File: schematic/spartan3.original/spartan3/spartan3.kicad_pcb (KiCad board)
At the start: 2 copper layers, 200 x 160 mm, 208 parts, among them U1_clk_select_0 SPFT_Sliding_Switch-dynacore, U2 XC3S250E-4TQG144C

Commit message: PCB layout :: updated
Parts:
- moved R_out_can_read_0 159.0 mm to (42.2, 5.08)
- moved R_out_can_write_0 139.3 mm to (83.8, 7.62)
- moved R_JTAG_TDO_0 133.7 mm to (152.4, 15.2)
- moved R_in_bus1_0 132.3 mm to (20.3, 55.9)
- moved R_eeprom_w_0 118.1 mm to (175.3, 7.62)
- moved R_eeprom_s_0 116.3 mm to (167.6, 15.2)
- moved R_in_write_reg_en_0 116.2 mm to (94.0, 12.7)
- moved R__eeprom_dq1_0 113.0 mm to (167.6, 20.3)
- moved R_out_clkr_0 110.1 mm to (12.7, 132.1)
- moved R_out_temp_w_0 108.1 mm to (208.3, 121.9)
- moved D_in_bus1_one_0 107.1 mm to (29.5, 96.5)
- moved R_in_is_clk_high_0 105.0 mm to (45.7, 151.9)
- moved R_in_clk_manual_0 102.6 mm to (45.7, 157.5)
- moved R_in_manual_input_r_0 97.9 mm to (185.4, 88.9)
- moved R_in_is_clk_low_0 97.2 mm to (45.7, 147.3)
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
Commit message: PCB layout :: updated
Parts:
- moved R_out_sysbus_6 231.5 mm to (224.5, 142.2)
- moved D_out_sysbus_6 213.9 mm to (236.2, 142.2)
- moved D_out_sysbus_4 213.1 mm to (236.2, 132.1)
- moved D_out_sysbus_2 211.6 mm to (236.2, 121.9)
- moved D_out_sysbus_0 209.4 mm to (235.2, 111.8)
- moved D_out_sysbus_7 208.2 mm to (235.2, 147.3)
- moved D_out_sysbus_3 204.1 mm to (235.2, 127.0)
- moved C_clk_1 197.3 mm to (213.4, 58.4)
- moved L_clk_0 196.4 mm to (221.0, 58.4)
- moved D_out_sysbus_5 191.5 mm to (236.2, 137.2)
- moved R_eeprom_hold_0 158.3 mm to (177.8, 2.54)
- moved D_out_r1_r_0 151.2 mm to (116.8, 236.2)
- moved D_in_manual_input_r_0 148.7 mm to (195.6, 185.4)
- moved D_out_ram_w_0 145.2 mm to (116.8, 243.8)
- moved D_out_acc_r_0 144.0 mm to (119.4, 251.5)
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
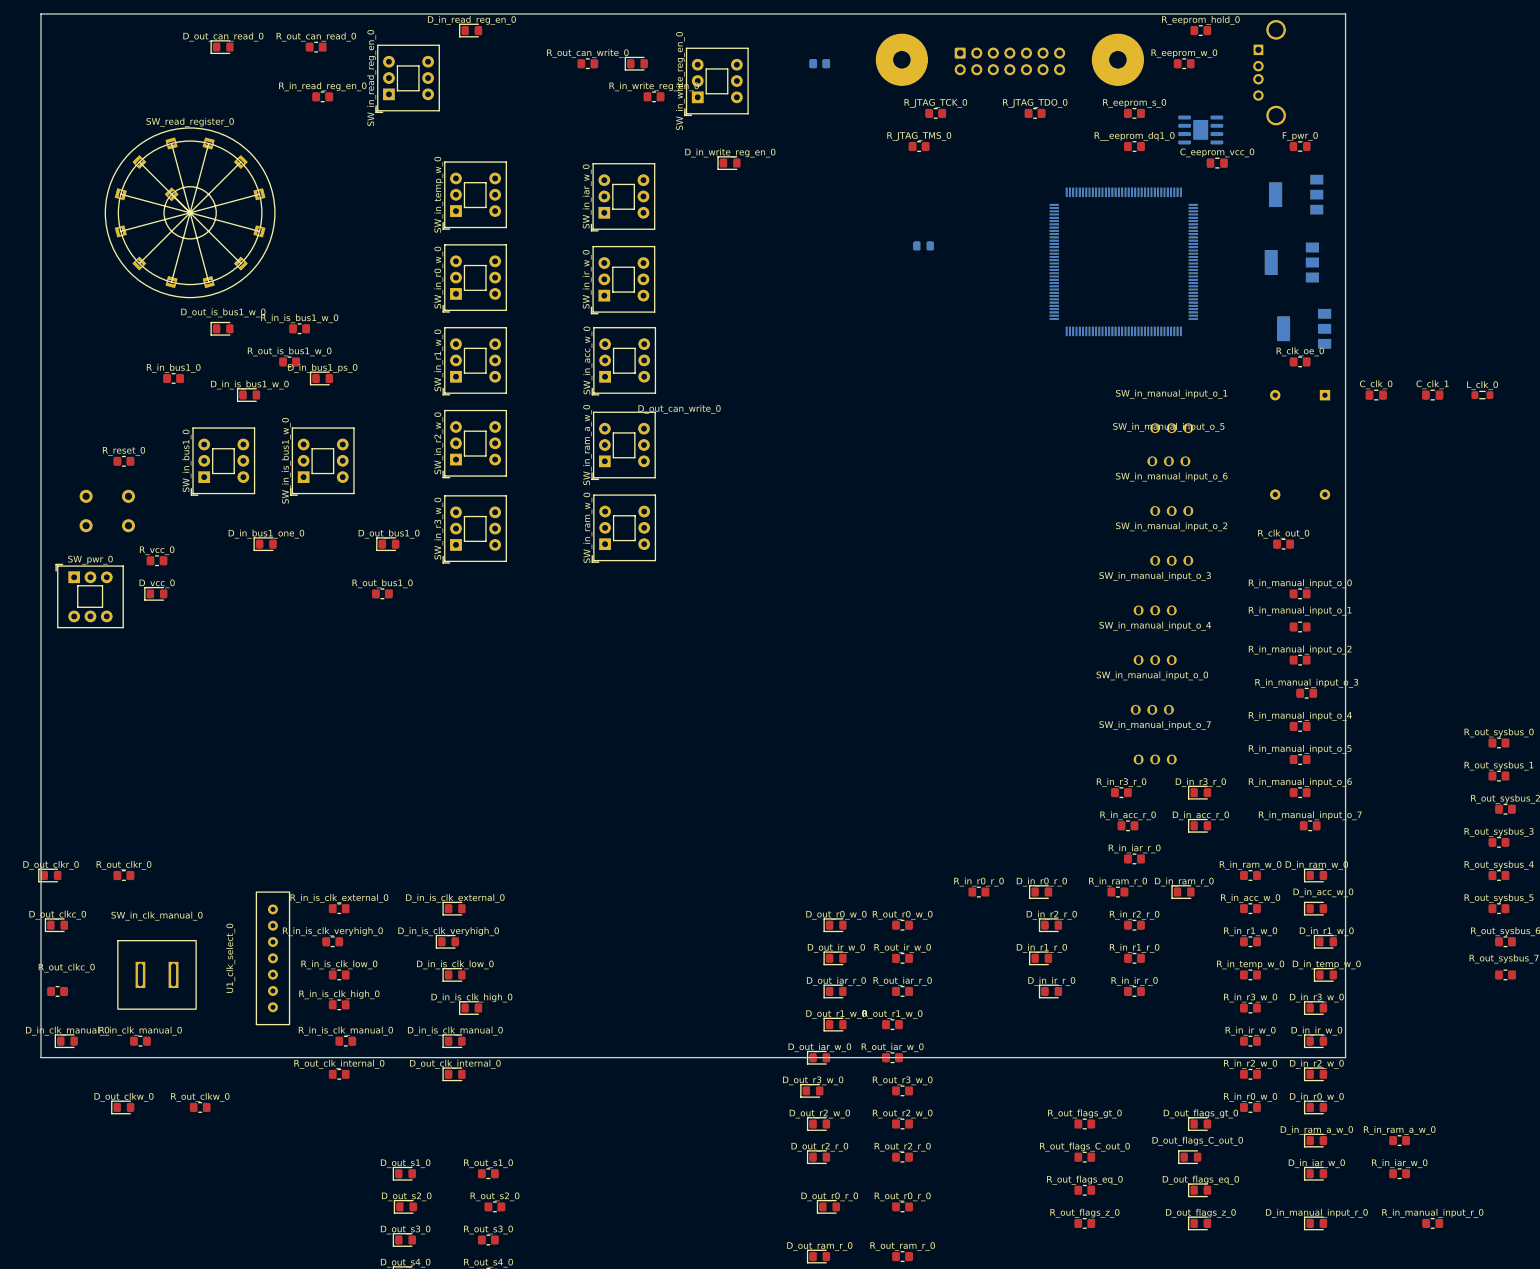
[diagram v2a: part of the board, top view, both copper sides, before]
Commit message: Schematics :: Read Register fixed -- Rs added. PCB layout :: Updated
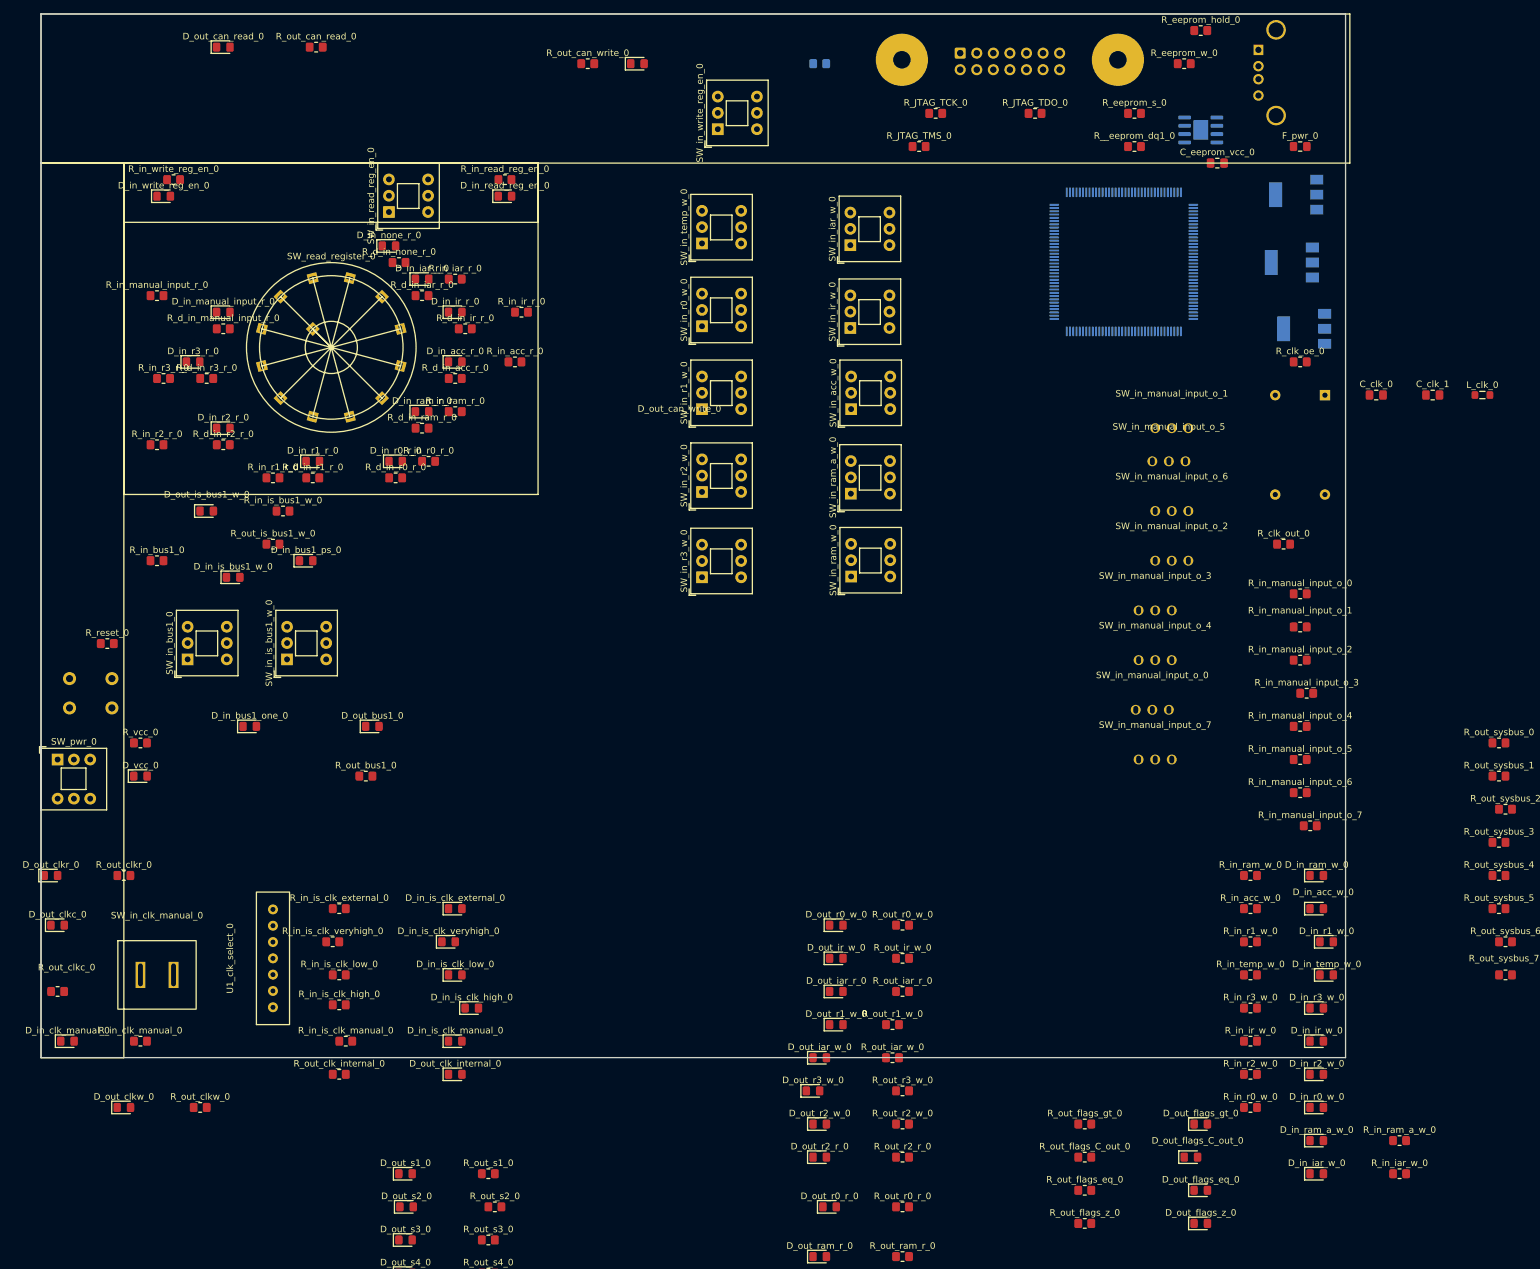
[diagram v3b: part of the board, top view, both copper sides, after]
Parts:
- added D_in_none_r_0: LED_Small, LED_SMD:LED_0805_2012Metric_Pad1.15x1.40mm_HandSolder, F.Cu at (53.3, 35.6)
- added R_d_in_acc_r_0: 100R, Resistor_SMD:R_0805_2012Metric_Pad1.20x1.40mm_HandSolder, F.Cu at (63.5, 55.9)
- added R_d_in_iar_r_0: 100R, Resistor_SMD:R_0805_2012Metric_Pad1.20x1.40mm_HandSolder, F.Cu at (58.4, 43.2)
- added R_d_in_ir_r_0: 100R, Resistor_SMD:R_0805_2012Metric_Pad1.20x1.40mm_HandSolder, F.Cu at (65.0, 48.3)
- added R_d_in_manual_input_r_0: 100R, Resistor_SMD:R_0805_2012Metric_Pad1.20x1.40mm_HandSolder, F.Cu at (27.9, 48.3)
- added R_d_in_none_r_0: 100R, Resistor_SMD:R_0805_2012Metric_Pad1.20x1.40mm_HandSolder, F.Cu at (54.9, 38.1)
- added R_d_in_r0_r_0: 100R, Resistor_SMD:R_0805_2012Metric_Pad1.20x1.40mm_HandSolder, F.Cu at (54.4, 71.1)
- added R_d_in_r1_r_0: 100R, Resistor_SMD:R_0805_2012Metric_Pad1.20x1.40mm_HandSolder, F.Cu at (41.7, 71.1)
- added R_d_in_r2_r_0: 100R, Resistor_SMD:R_0805_2012Metric_Pad1.20x1.40mm_HandSolder, F.Cu at (27.9, 66.0)
- added R_d_in_r3_r_0: 100R, Resistor_SMD:R_0805_2012Metric_Pad1.20x1.40mm_HandSolder, F.Cu at (25.4, 55.9)
- added R_d_in_ram_r_0: 100R, Resistor_SMD:R_0805_2012Metric_Pad1.20x1.40mm_HandSolder, F.Cu at (58.4, 63.5)
- D_in_iar_r_0: moved to F.Cu
- moved R_in_manual_input_r_0 241.8 mm to (17.8, 43.2)
- moved D_in_manual_input_r_0 218.2 mm to (27.9, 45.7)
- moved D_in_r3_r_0 168.0 mm to (23.3, 53.3)
- moved R_in_r2_r_0 167.0 mm to (17.8, 66.0)
- moved R_in_r3_r_0 160.0 mm to (18.8, 55.9)
- moved R_in_r1_r_0 151.2 mm to (35.6, 71.1)
- moved D_in_r2_r_0 148.1 mm to (27.9, 63.5)
- moved R_in_ir_r_0 140.3 mm to (73.7, 45.7)
- moved D_in_ir_r_0 138.6 mm to (63.5, 45.7)
- moved D_in_ram_r_0 138.1 mm to (58.4, 61.0)
- moved R_in_iar_r_0 136.9 mm to (63.5, 40.6)
- moved D_in_r1_r_0 135.3 mm to (41.7, 68.6)
- moved D_in_acc_r_0 134.6 mm to (63.5, 53.3)
- moved R_in_ram_r_0 125.5 mm to (63.5, 61.0)
- moved D_in_r0_r_0 119.1 mm to (54.4, 68.6)
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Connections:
- D_in_acc_r_0 pad 2: VCC -> Net-(D_in_acc_r_0-Pad2)
- D_in_iar_r_0 pad 2: VCC -> Net-(D_in_iar_r_0-Pad2)
- D_in_ir_r_0 pad 2: VCC -> Net-(D_in_ir_r_0-Pad2)
- D_in_manual_input_r_0 pad 2: VCC -> Net-(D_in_manual_input_r_0-Pad2)
- D_in_r0_r_0 pad 2: VCC -> Net-(D_in_r0_r_0-Pad2)
- D_in_r1_r_0 pad 2: VCC -> Net-(D_in_r1_r_0-Pad2)
- D_in_r2_r_0 pad 2: VCC -> Net-(D_in_r2_r_0-Pad2)
- D_in_r3_r_0 pad 2: VCC -> Net-(D_in_r3_r_0-Pad2)
- D_in_ram_r_0 pad 2: VCC -> Net-(D_in_ram_r_0-Pad2)
- SW_read_register_0 pad 1: in_iar_r -> in_manual_input_r
- SW_read_register_0 pad 10: unconnected-(SW_read_register_0-Pad10) -> in_r1_r
- SW_read_register_0 pad 11: unconnected-(SW_read_register_0-Pad11) -> in_r2_r
- SW_read_register_0 pad 12: unconnected-(SW_read_register_0-Pad12) -> in_r3_r
- SW_read_register_0 pad 2: in_ir_r -> unconnected-(SW_read_register_0-Pad2)
- SW_read_register_0 pad 3: in_acc_r -> unconnected-(SW_read_register_0-Pad3)
- SW_read_register_0 pad 4: in_ram_r -> Net-(D_in_none_r_0-Pad1)
- SW_read_register_0 pad 5: in_r0_r -> in_iar_r
- SW_read_register_0 pad 6: in_r1_r -> in_ir_r
- SW_read_register_0 pad 7: in_r2_r -> in_acc_r
- SW_read_register_0 pad 8: in_r3_r -> in_ram_r
- SW_read_register_0 pad 9: in_manual_input_r -> in_r0_r

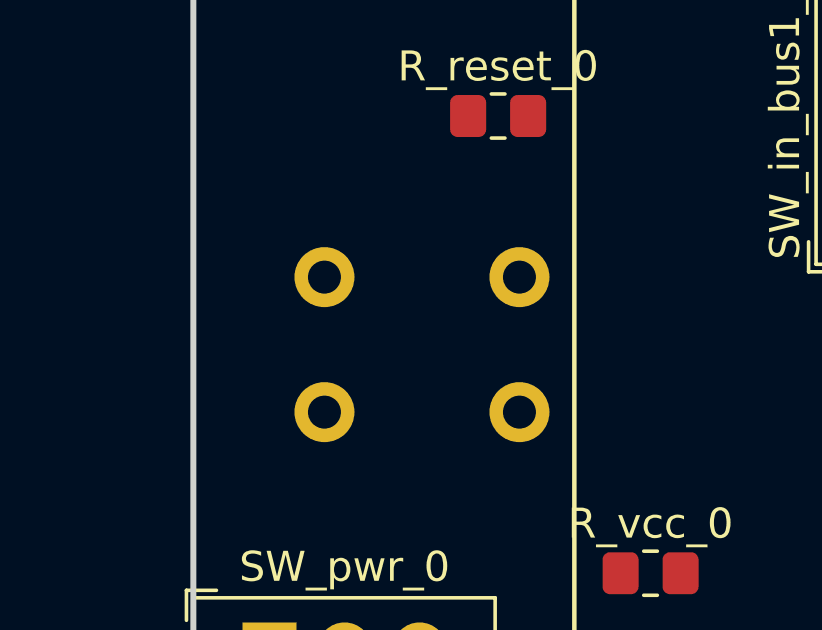
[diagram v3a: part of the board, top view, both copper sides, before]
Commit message: PCB layout :: reset button side swapped
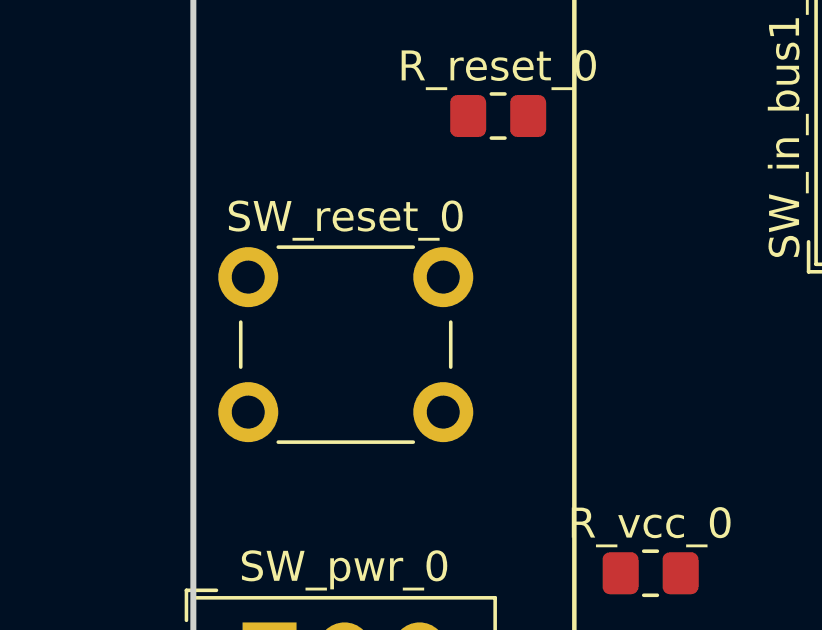
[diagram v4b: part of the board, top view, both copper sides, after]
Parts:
- SW_reset_0: moved to F.Cu
- moved SW_reset_0 9.04 mm to (1.83, 101.9), turned to 0 degrees
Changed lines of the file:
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@@
+    )
+  )
+  (footprint "Button_Switch_THT:SW_PUSH_6mm_H9.5mm" (layer "F.Cu")
+    (at 1.83 101.89)
+    (descr "tactile push button, 6x6mm e.g. PHAP33xx series, height=9.5mm")
+    (tags "tact sw push 6mm")
+    (property "Sheetfile" "spartan3.kicad_sch")
+    (property "Sheetname" "")
+    (attr through_hole)
+    (fp_text reference "SW_reset_0" (at 3.25 -2) (layer "F.SilkS")
+      (effects (font (size 1 1) (thickness 0.15)))
+    )
+    (fp_text value "SW_Push" (at 3.75 6.7) (layer "F.Fab")
+      (effects (font (size 1 1) (thickness 0.15)))
+    )
+    (fp_text user "${REFERENCE}" (at 3.25 2.25) (layer "F.Fab")
+      (effects (font (size 1 1) (thickness 0.15)))
+    )
+    (fp_line (start 6.75 3) (end 6.75 1.5) (layer "F.SilkS") (width 0.12))
+    (fp_line (start 1 5.5) (end 5.5 5.5) (layer "F.SilkS") (width 0.12))
+    (fp_line (start 5.5 -1) (end 1 -1) (layer "F.SilkS") (width 0.12))
+    (fp_line (start -0.25 1.5) (end -0.25 3) (layer "F.SilkS") (width 0.12))
+    (fp_line (start -1.5 5.75) (end -1.5 -1.25) (layer "F.CrtYd") (width 0.05))
+    (fp_line (start 8 -1.5) (end 8 -1.25) (layer "F.CrtYd") (width 0.05))
+    (fp_line (start -1.5 6) (end -1.25 6) (layer "F.CrtYd") (width 0.05))
+    (fp_line (start 7.75 6) (end -1.25 6) (layer "F.CrtYd") (width 0.05))
+    (fp_line (start 8 -1.25) (end 8 5.75) (layer "F.CrtYd") (width 0.05))
+    (fp_line (start -1.25 -1.5) (end 7.75 -1.5) (layer "F.CrtYd") (width 0.05))
+    (fp_line (start 7.75 6) (end 8 6) (layer "F.CrtYd") (width 0.05))
+    (fp_line (start -1.5 -1.5) (end -1.25 -1.5) (layer "F.CrtYd") (width 0.05))
+    (fp_line (start -1.5 5.75) (end -1.5 6) (layer "F.CrtYd") (width 0.05))
+    (fp_line (start 8 6) (end 8 5.75) (layer "F.CrtYd") (width 0.05))
+    (fp_line (start 7.75 -1.5) (end 8 -1.5) (layer "F.CrtYd") (width 0.05))
+    (fp_line (start -1.5 -1.25) (end -1.5 -1.5) (layer "F.CrtYd") (width 0.05))
+    (fp_line (start 6.25 -0.75) (end 6.25 5.25) (layer "F.Fab") (width 0.1))
+    (fp_line (start 0.25 -0.75) (end 3.25 -0.75) (layer "F.Fab") (width 0.1))
+    (fp_line (start 0.25 5.25) (end 0.25 -0.75) (layer "F.Fab") (width 0.1))
+    (fp_line (start 3.25 -0.75) (end 6.25 -0.75) (layer "F.Fab") (width 0.1))
+    (fp_line (start 6.25 5.25) (end 0.25 5.25) (layer "F.Fab") (width 0.1))
+    (fp_circle (center 3.25 2.25) (end 1.25 2.5) (layer "F.Fab") (width 0.1) (fill none))
+    (pad "1" thru_hole circle (at 6.5 0 90) (size 2 2) (drill 1.1) (layers *.Cu *.Mask)
+      (net 152 "reset") (pinfunction "1") (pintype "passive"))
+    (pad "1" thru_hole circle (at 0 0 90) (size 2 2) (drill 1.1) (layers *.Cu *.Mask)
+      (net 152 "reset") (pinfunction "1") (pintype "passive"))
+    (pad "2" thru_hole circle (at 0 4.5 90) (size 2 2) (drill 1.1) (layers *.Cu *.Mask)
+      (net 2 "GND") (pinfunction "2") (pintype "passive"))
+    (pad "2" thru_hole circle (at 6.5 4.5 90) (size 2 2) (drill 1.1) (layers *.Cu *.Mask)
+      (net 2 "GND") (pinfunction "2") (pintype "passive"))
+    (model "${KICAD6_3DMODEL_DIR}/Button_Switch_THT.3dshapes/SW_PUSH_6mm_H9.5mm.wrl"
+      (offset (xyz 0 0 0))
+      (scale (xyz 1 1 1))
+      (rotate (xyz 0 0 0))
     )
   )
@@
       (offset (xyz 0 0 0))
       (scale (xyz 1 1 1))
-      (rotate (xyz 0 0 0))
-    )
-  )
-  (footprint "Button_Switch_THT:SW_PUSH_6mm_H9.5mm" (layer "B.Cu")
-    (at 10.87 101.89 180)
-    (descr "tactile push button, 6x6mm e.g. PHAP33xx series, height=9.5mm")
-    (tags "tact sw push 6mm")
-    (property "Sheetfile" "spartan3.kicad_sch")
-    (property "Sheetname" "")
-    (attr through_hole)
-    (fp_text reference "SW_reset_0" (at 3.25 2) (layer "B.SilkS")
-      (effects (font (size 1 1) (thickness 0.15)) (justify mirror))
-    )
-    (fp_text value "SW_Push" (at 3.75 -6.7) (layer "B.Fab")
-      (effects (font (size 1 1) (thickness 0.15)) (justify mirror))
-    )
-    (fp_text user "${REFERENCE}" (at 3.25 -2.25) (layer "B.Fab")
-      (effects (font (size 1 1) (thickness 0.15)) (justify mirror))
-    )
-    (fp_line (start 6.75 -3) (end 6.75 -1.5) (layer "B.SilkS") (width 0.12))
-    (fp_line (start 1 -5.5) (end 5.5 -5.5) (layer "B.SilkS") (width 0.12))
-    (fp_line (start 5.5 1) (end 1 1) (layer "B.SilkS") (width 0.12))
-    (fp_line (start -0.25 -1.5) (end -0.25 -3) (layer "B.SilkS") (width 0.12))
-    (fp_line (start -1.5 -5.75) (end -1.5 1.25) (layer "B.CrtYd") (width 0.05))
-    (fp_line (start 8 1.5) (end 8 1.25) (layer "B.CrtYd") (width 0.05))
-    (fp_line (start -1.5 -6) (end -1.25 -6) (layer "B.CrtYd") (width 0.05))
-    (fp_line (start 7.75 -6) (end -1.25 -6) (layer "B.CrtYd") (width 0.05))
-    (fp_line (start 8 1.25) (end 8 -5.75) (layer "B.CrtYd") (width 0.05))
-    (fp_line (start -1.25 1.5) (end 7.75 1.5) (layer "B.CrtYd") (width 0.05))
-    (fp_line (start 7.75 -6) (end 8 -6) (layer "B.CrtYd") (width 0.05))
-    (fp_line (start -1.5 1.5) (end -1.25 1.5) (layer "B.CrtYd") (width 0.05))
-    (fp_line (start -1.5 -5.75) (end -1.5 -6) (layer "B.CrtYd") (width 0.05))
-    (fp_line (start 8 -6) (end 8 -5.75) (layer "B.CrtYd") (width 0.05))
-    (fp_line (start 7.75 1.5) (end 8 1.5) (layer "B.CrtYd") (width 0.05))
-    (fp_line (start -1.5 1.25) (end -1.5 1.5) (layer "B.CrtYd") (width 0.05))
-    (fp_line (start 6.25 0.75) (end 6.25 -5.25) (layer "B.Fab") (width 0.1))
-    (fp_line (start 0.25 0.75) (end 3.25 0.75) (layer "B.Fab") (width 0.1))
-    (fp_line (start 0.25 -5.25) (end 0.25 0.75) (layer "B.Fab") (width 0.1))
-    (fp_line (start 3.25 0.75) (end 6.25 0.75) (layer "B.Fab") (width 0.1))
-    (fp_line (start 6.25 -5.25) (end 0.25 -5.25) (layer "B.Fab") (width 0.1))
-    (fp_circle (center 3.25 -2.25) (end 1.25 -2.5) (layer "B.Fab") (width 0.1) (fill none))
-    (pad "1" thru_hole circle (at 6.5 0 90) (size 2 2) (drill 1.1) (layers *.Cu *.Mask)
-      (net 152 "reset") (pinfunction "1") (pintype "passive"))
-    (pad "1" thru_hole circle (at 0 0 90) (size 2 2) (drill 1.1) (layers *.Cu *.Mask)
-      (net 152 "reset") (pinfunction "1") (pintype "passive"))
-    (pad "2" thru_hole circle (at 0 -4.5 90) (size 2 2) (drill 1.1) (layers *.Cu *.Mask)
-      (net 2 "GND") (pinfunction "2") (pintype "passive"))
-    (pad "2" thru_hole circle (at 6.5 -4.5 90) (size 2 2) (drill 1.1) (layers *.Cu *.Mask)
-      (net 2 "GND") (pinfunction "2") (pintype "passive"))
-    (model "${KICAD6_3DMODEL_DIR}/Button_Switch_THT.3dshapes/SW_PUSH_6mm_H9.5mm.wrl"
-      (offset (xyz 0 0 0))
-      (scale (xyz 1 1 1))
